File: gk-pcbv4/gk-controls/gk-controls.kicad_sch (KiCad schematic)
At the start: 34 parts, among them J1 Conn_01x20, U1 PCAL6416APW, U2 ULN2003A

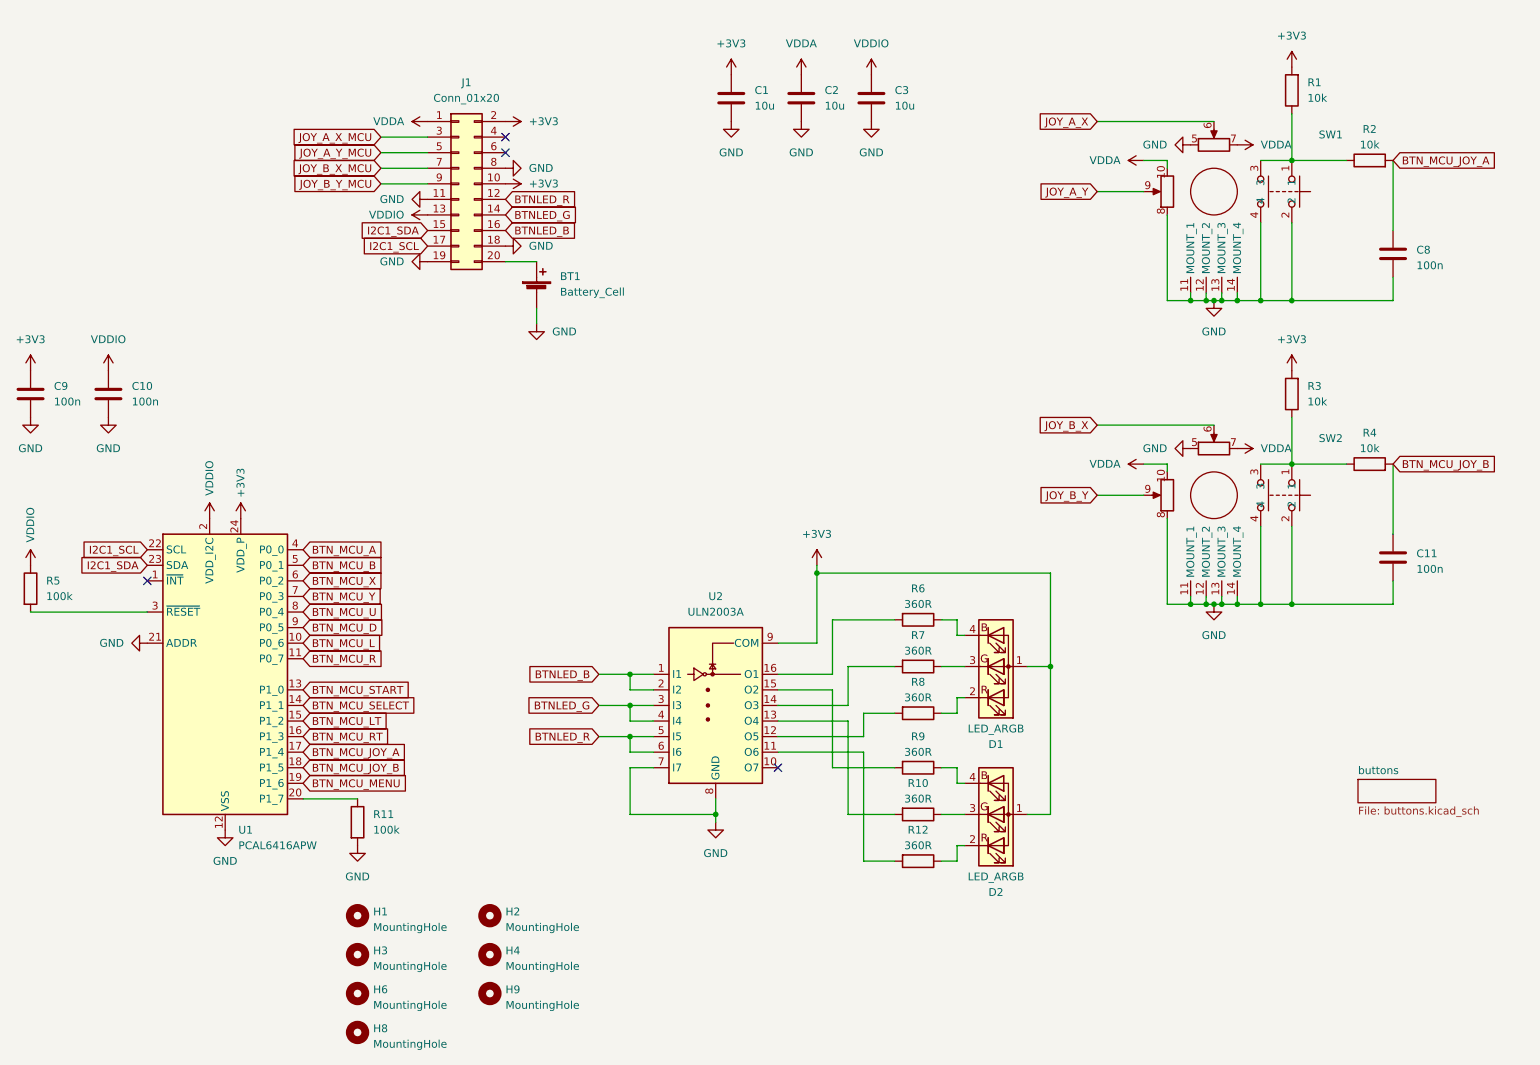
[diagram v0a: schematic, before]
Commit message: add oled screens in abxy buttons and support pcb for these
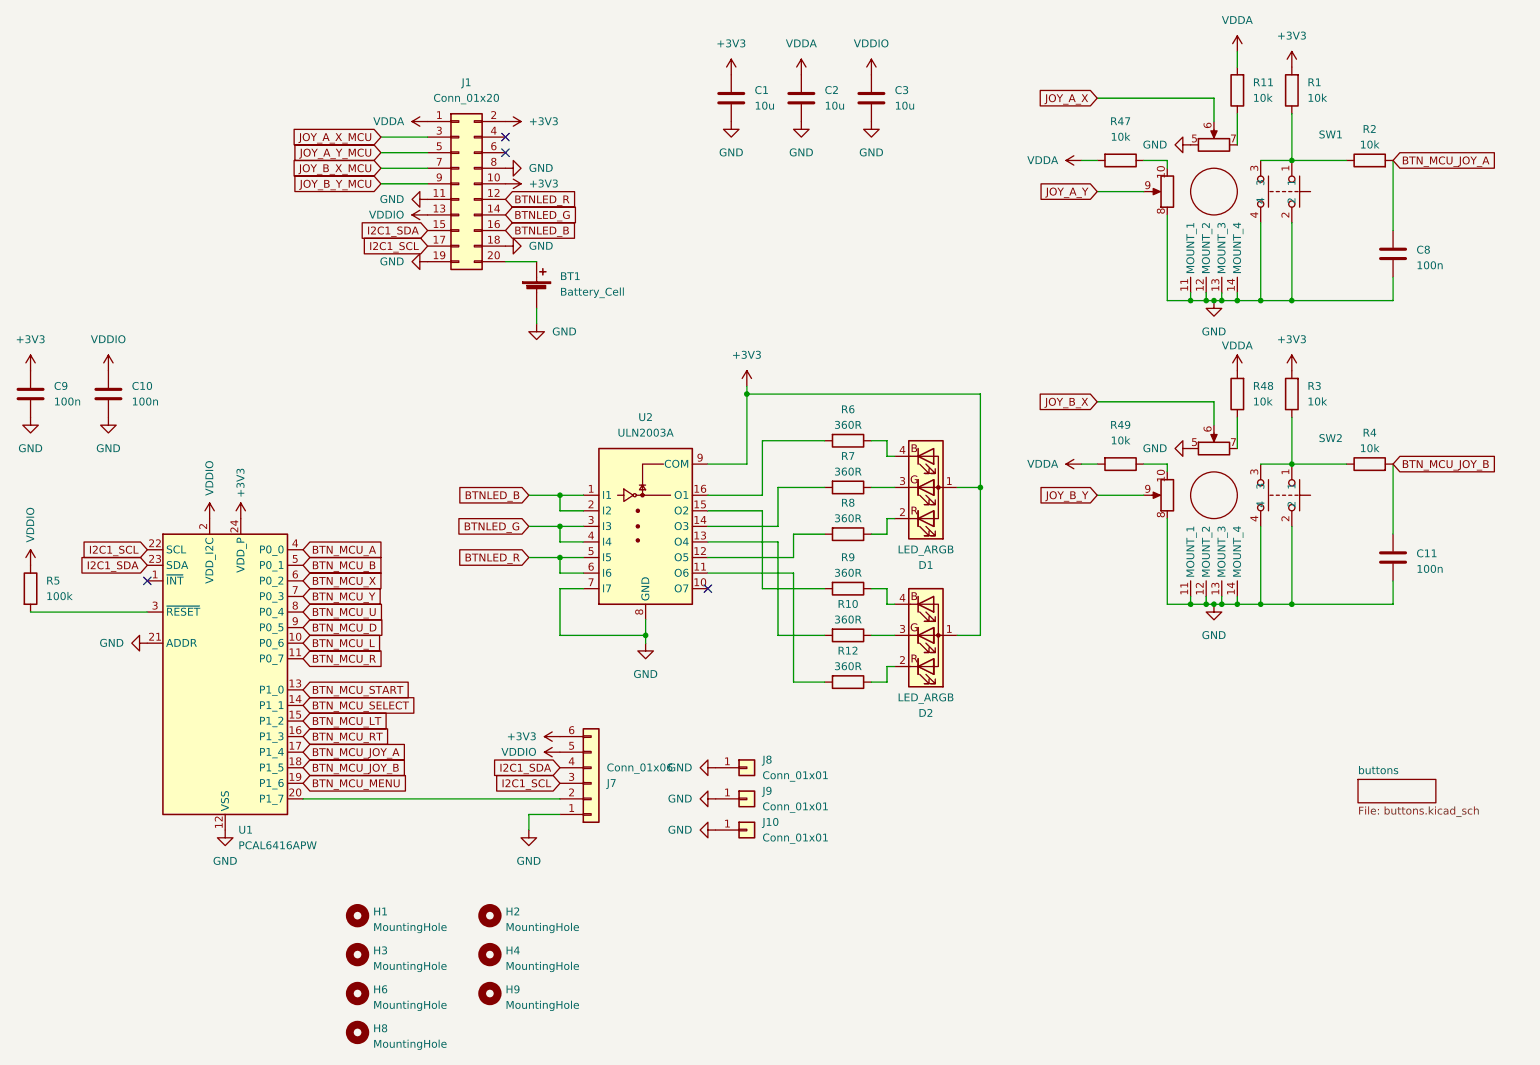
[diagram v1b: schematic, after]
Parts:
- added J10, J8, J9: Conn_01x01, Connector_PinHeader_2.54mm:PinHeader_1x01_P2.54mm_Vertical, symbol Connector_Generic:Conn_01x01
- added J7: Conn_01x06, Connector_FFC-FPC:TE_0-1734839-6_1x06-1MP_P0.5mm_Horizontal, symbol Connector_Generic:Conn_01x06
- added R47, R48, R49: 10k, Resistor_SMD:R_0603_1608Metric, symbol Device:R
- R11: value 100k -> 10k
- SW1, SW2: value ~ -> (none)
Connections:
- net +3V3: now also J7.6 (Pin_6)
- net GND: now also J10.1 (Pin_1), J7.1 (Pin_1), J8.1 (Pin_1), J9.1 (Pin_1); no longer R11.2
- net I2C1_SCL: now also J7.3 (Pin_3)
- net I2C1_SDA: now also J7.4 (Pin_4)
- net VDDA: now also R11.2, R47.2, R48.2, R49.2; no longer SW1.10, SW1.7, SW2.10, SW2.7
- net VDDIO: now also J7.5 (Pin_5)
- net at U1.20 (P1_7): now also J7.2 (Pin_2); no longer R11.1
- new net: R48.1, SW2.7
- new net: R47.1, SW1.10
- new net: R11.1, SW1.7
- new net: R49.1, SW2.10
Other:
- moved on the sheet: D1, D2, R10, R12, R6, R7, R8, R9, U2
